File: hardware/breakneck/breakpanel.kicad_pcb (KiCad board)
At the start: 2 copper layers, 145 x 165 mm, 690 parts, among them J1 CONN_WEST, J10 GS2, J12 CONN_JTAG_6P, J15 GS2, J16 CONN_JST, J2 CONN_DEDI, J3 CONN_OLED, J4 USB_C_Receptacle, J5 CONN_SOUTH, J6 CONN_EAST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

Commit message: Flushed current changes to accommodate results of recent assembly tests; Introduced plastics engineering resources, made fiducial marks SMT for placing, merged SMT attribute to panel design accordingly, removed incomplete test point symbol, and sanitised private file path.
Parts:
- FID2 (x6), FID4 (x6), FID6 (x5): footprint Monero_Local:Fiducial_1mm_Dia_2.54mm_Outer_CopperBottom -> Monero_Local:Fiducial_1mm_Dia_2.54mm_Outer_CopperTop; moved to B.Cu
- turned FID2 to 270 degrees (x6)
- turned FID4 to 270 degrees (x6)
- turned FID6 to 270 degrees (x3)
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
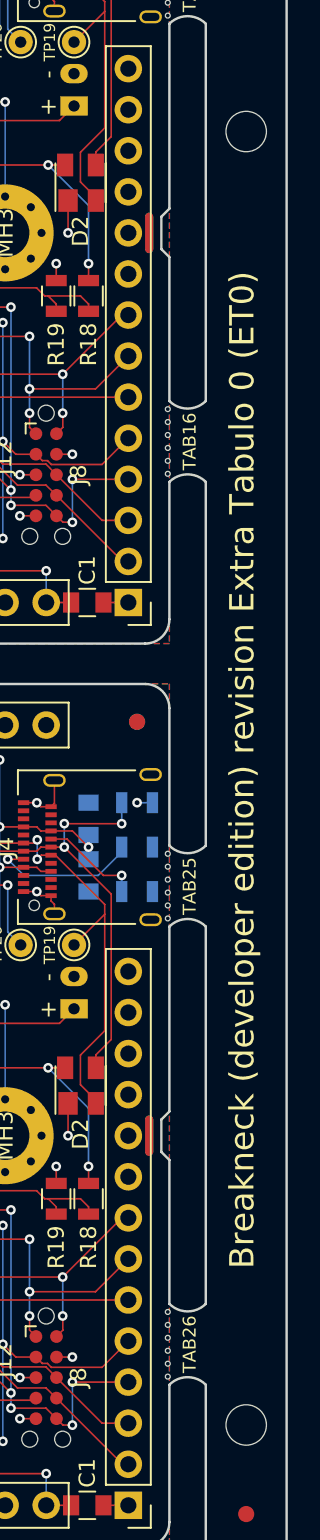
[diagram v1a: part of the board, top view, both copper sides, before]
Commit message: Completed USBC debugging structures, including removal of unused contacts, symbol adaptation, introduction of solderbridges, test point connections, and complete segregation of inner row USBC connector pads.
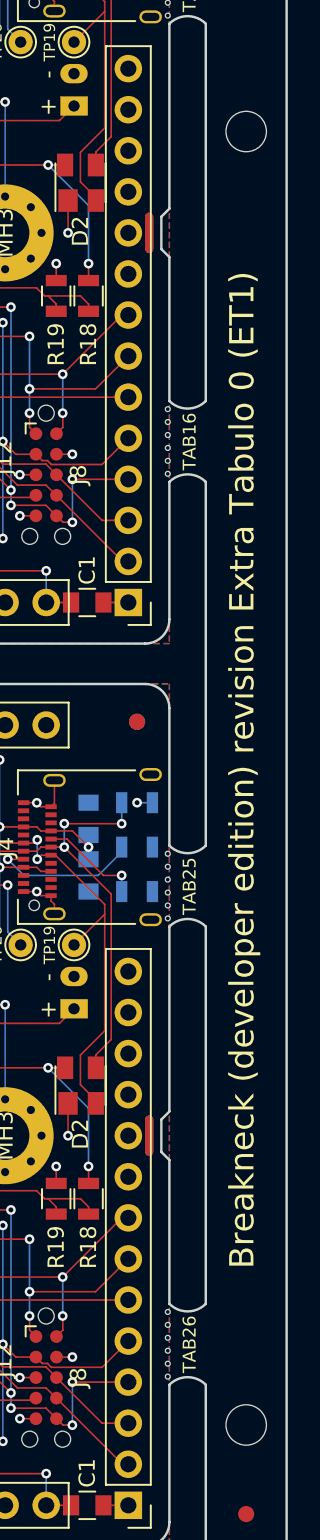
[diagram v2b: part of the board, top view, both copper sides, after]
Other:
- board text added: "Breakneck (developer edition) revision Extra Tabulo 0 (ET1)"
- board text added: "Fifth generation prototype RFC-HWALLET-1 ET1 Extra Tabulo, by the Monero Hardware Team CERN OSH License, © 2018 The Monero Project"
- board text removed: "Breakneck (developer edition) revision Extra Tabulo 0 (ET0)"
- board text removed: "Fifth generation prototype RFC-HWALLET-1 ET0 Extra Tabulo, by the Monero Hardware Team CERN OSH License, © 2018 The Monero Project"
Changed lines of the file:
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@@
     (title "Breakneck Hardware Wallet")
     (date 2018-01-10)
-    (rev 0.9.0)
+    (rev 0.9.1)
     (company "The Monero Project, Hardware Team")
     (comment 1 "Copyright © 2018, The Monero Project")
@@
     (effects (font (size 1.5 1.5) (thickness 0.3)))
   )
-  (gr_text "Breakneck (developer edition) revision Extra Tabulo 0 (ET0)" (at 165 137 90) (layer F.SilkS)
+  (gr_text "Breakneck (developer edition) revision Extra Tabulo 0 (ET1)" (at 165 137 90) (layer F.SilkS)
     (effects (font (size 1.5 1.5) (thickness 0.3)))
   )
@@
   (gr_line (start 36 132.68) (end 34 132.68) (angle 90) (layer Edge.Cuts) (width 0.15))
   (gr_line (start 34 132.68) (end 33 131.68) (angle 90) (layer Edge.Cuts) (width 0.15))
-  (gr_text "Fifth generation prototype RFC-HWALLET-1\nET0 Extra Tabulo, by the Monero Hardware Team\nCERN OSH License, © 2018 The Monero Project" (at 53 140.02 90) (layer B.SilkS)
+  (gr_text "Fifth generation prototype RFC-HWALLET-1\nET1 Extra Tabulo, by the Monero Hardware Team\nCERN OSH License, © 2018 The Monero Project" (at 53 140.02 90) (layer B.SilkS)
     (effects (font (size 1 1) (thickness 0.2)) (justify left mirror))
   )
@@
   (gr_line (start 102.5 132.68) (end 100.5 132.68) (angle 90) (layer Edge.Cuts) (width 0.15))
   (gr_line (start 100.5 132.68) (end 99.5 131.68) (angle 90) (layer Edge.Cuts) (width 0.15))
-  (gr_text "Fifth generation prototype RFC-HWALLET-1\nET0 Extra Tabulo, by the Monero Hardware Team\nCERN OSH License, © 2018 The Monero Project" (at 119.5 140.02 90) (layer B.SilkS)
+  (gr_text "Fifth generation prototype RFC-HWALLET-1\nET1 Extra Tabulo, by the Monero Hardware Team\nCERN OSH License, © 2018 The Monero Project" (at 119.5 140.02 90) (layer B.SilkS)
     (effects (font (size 1 1) (thickness 0.2)) (justify left mirror))
   )
@@
   (gr_line (start 102.5 76.84) (end 100.5 76.84) (angle 90) (layer Edge.Cuts) (width 0.15))
   (gr_line (start 100.5 76.84) (end 99.5 75.84) (angle 90) (layer Edge.Cuts) (width 0.15))
-  (gr_text "Fifth generation prototype RFC-HWALLET-1\nET0 Extra Tabulo, by the Monero Hardware Team\nCERN OSH License, © 2018 The Monero Project" (at 119.5 84.18 90) (layer B.SilkS)
+  (gr_text "Fifth generation prototype RFC-HWALLET-1\nET1 Extra Tabulo, by the Monero Hardware Team\nCERN OSH License, © 2018 The Monero Project" (at 119.5 84.18 90) (layer B.SilkS)
     (effects (font (size 1 1) (thickness 0.2)) (justify left mirror))
   )
@@
   (gr_line (start 160 48.94) (end 160 46.94) (angle 90) (layer Edge.Cuts) (width 0.15))
   (gr_line (start 160 46.94) (end 160.5 46.44) (angle 90) (layer Edge.Cuts) (width 0.15))
-  (gr_text "Fifth generation prototype RFC-HWALLET-1\nET0 Extra Tabulo, by the Monero Hardware Team\nCERN OSH License, © 2018 The Monero Project" (at 119.5 28.34 90) (layer B.SilkS)
+  (gr_text "Fifth generation prototype RFC-HWALLET-1\nET1 Extra Tabulo, by the Monero Hardware Team\nCERN OSH License, © 2018 The Monero Project" (at 119.5 28.34 90) (layer B.SilkS)
     (effects (font (size 1 1) (thickness 0.2)) (justify left mirror))
   )
@@
   (gr_line (start 36 21) (end 34 21) (angle 90) (layer Edge.Cuts) (width 0.15))
   (gr_line (start 34 21) (end 33 20) (angle 90) (layer Edge.Cuts) (width 0.15))
-  (gr_text "Fifth generation prototype RFC-HWALLET-1\nET0 Extra Tabulo, by the Monero Hardware Team\nCERN OSH License, © 2018 The Monero Project" (at 53 28.34 90) (layer B.SilkS)
+  (gr_text "Fifth generation prototype RFC-HWALLET-1\nET1 Extra Tabulo, by the Monero Hardware Team\nCERN OSH License, © 2018 The Monero Project" (at 53 28.34 90) (layer B.SilkS)
     (effects (font (size 1 1) (thickness 0.2)) (justify left mirror))
   )
@@
     (effects (font (size 1 1) (thickness 0.15)))
   )
-  (gr_text "Fifth generation prototype RFC-HWALLET-1\nET0 Extra Tabulo, by the Monero Hardware Team\nCERN OSH License, © 2018 The Monero Project" (at 53 84.18 90) (layer B.SilkS)
+  (gr_text "Fifth generation prototype RFC-HWALLET-1\nET1 Extra Tabulo, by the Monero Hardware Team\nCERN OSH License, © 2018 The Monero Project" (at 53 84.18 90) (layer B.SilkS)
     (effects (font (size 1 1) (thickness 0.2)) (justify left mirror))
   )

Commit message: Bumped revision identifiers and legal text pending new year of the pig.
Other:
- board text added: "Panelised by the Monero Hardware team, January 2019"
- board text added: "Seventh generation prototype RFC-HWALLET-1 ET1 Extra Tabulo, by the Monero Hardware Team CERN OSH License, © 2019 The Monero Project"
- board text removed: "Fifth generation prototype RFC-HWALLET-1 ET1 Extra Tabulo, by the Monero Hardware Team CERN OSH License, © 2018 The Monero Project"
- board text removed: "Panelised by the Monero Hardware team, 6 December 2018"
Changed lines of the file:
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@@
     (title "Breakneck Hardware Wallet")
     (date 2018-01-10)
-    (rev 0.9.1)
+    (rev 0.9.2)
     (company "The Monero Project, Hardware Team")
-    (comment 1 "Copyright © 2018, The Monero Project")
+    (comment 1 "Copyright © 2019, The Monero Project")
     (comment 2 "Fulfilling the developer edition role")
     (comment 3 "Pending quality assurance testing")
@@
     (effects (font (size 1.5 1.5) (thickness 0.3)))
   )
-  (gr_text "Panelised by the Monero Hardware team, 6 December 2018" (at 25 138 90) (layer F.SilkS)
+  (gr_text "Panelised by the Monero Hardware team, January 2019" (at 25 138 90) (layer F.SilkS)
     (effects (font (size 1.5 1.5) (thickness 0.3)))
   )
@@
   (gr_line (start 36 132.68) (end 34 132.68) (angle 90) (layer Edge.Cuts) (width 0.15))
   (gr_line (start 34 132.68) (end 33 131.68) (angle 90) (layer Edge.Cuts) (width 0.15))
-  (gr_text "Fifth generation prototype RFC-HWALLET-1\nET1 Extra Tabulo, by the Monero Hardware Team\nCERN OSH License, © 2018 The Monero Project" (at 53 140.02 90) (layer B.SilkS)
+  (gr_text "Seventh generation prototype RFC-HWALLET-1\nET1 Extra Tabulo, by the Monero Hardware Team\nCERN OSH License, © 2019 The Monero Project" (at 53 140.02 90) (layer B.SilkS)
     (effects (font (size 1 1) (thickness 0.2)) (justify left mirror))
   )
@@
   (gr_line (start 102.5 132.68) (end 100.5 132.68) (angle 90) (layer Edge.Cuts) (width 0.15))
   (gr_line (start 100.5 132.68) (end 99.5 131.68) (angle 90) (layer Edge.Cuts) (width 0.15))
-  (gr_text "Fifth generation prototype RFC-HWALLET-1\nET1 Extra Tabulo, by the Monero Hardware Team\nCERN OSH License, © 2018 The Monero Project" (at 119.5 140.02 90) (layer B.SilkS)
+  (gr_text "Seventh generation prototype RFC-HWALLET-1\nET1 Extra Tabulo, by the Monero Hardware Team\nCERN OSH License, © 2019 The Monero Project" (at 119.5 140.02 90) (layer B.SilkS)
     (effects (font (size 1 1) (thickness 0.2)) (justify left mirror))
   )
@@
   (gr_line (start 102.5 76.84) (end 100.5 76.84) (angle 90) (layer Edge.Cuts) (width 0.15))
   (gr_line (start 100.5 76.84) (end 99.5 75.84) (angle 90) (layer Edge.Cuts) (width 0.15))
-  (gr_text "Fifth generation prototype RFC-HWALLET-1\nET1 Extra Tabulo, by the Monero Hardware Team\nCERN OSH License, © 2018 The Monero Project" (at 119.5 84.18 90) (layer B.SilkS)
+  (gr_text "Seventh generation prototype RFC-HWALLET-1\nET1 Extra Tabulo, by the Monero Hardware Team\nCERN OSH License, © 2019 The Monero Project" (at 119.5 84.18 90) (layer B.SilkS)
     (effects (font (size 1 1) (thickness 0.2)) (justify left mirror))
   )
@@
   (gr_line (start 160 48.94) (end 160 46.94) (angle 90) (layer Edge.Cuts) (width 0.15))
   (gr_line (start 160 46.94) (end 160.5 46.44) (angle 90) (layer Edge.Cuts) (width 0.15))
-  (gr_text "Fifth generation prototype RFC-HWALLET-1\nET1 Extra Tabulo, by the Monero Hardware Team\nCERN OSH License, © 2018 The Monero Project" (at 119.5 28.34 90) (layer B.SilkS)
+  (gr_text "Seventh generation prototype RFC-HWALLET-1\nET1 Extra Tabulo, by the Monero Hardware Team\nCERN OSH License, © 2019 The Monero Project" (at 119.5 28.34 90) (layer B.SilkS)
     (effects (font (size 1 1) (thickness 0.2)) (justify left mirror))
   )
@@
   (gr_line (start 36 21) (end 34 21) (angle 90) (layer Edge.Cuts) (width 0.15))
   (gr_line (start 34 21) (end 33 20) (angle 90) (layer Edge.Cuts) (width 0.15))
-  (gr_text "Fifth generation prototype RFC-HWALLET-1\nET1 Extra Tabulo, by the Monero Hardware Team\nCERN OSH License, © 2018 The Monero Project" (at 53 28.34 90) (layer B.SilkS)
+  (gr_text "Seventh generation prototype RFC-HWALLET-1\nET1 Extra Tabulo, by the Monero Hardware Team\nCERN OSH License, © 2019 The Monero Project" (at 53 28.34 90) (layer B.SilkS)
     (effects (font (size 1 1) (thickness 0.2)) (justify left mirror))
   )
@@
     (effects (font (size 1 1) (thickness 0.15)))
   )
-  (gr_text "Fifth generation prototype RFC-HWALLET-1\nET1 Extra Tabulo, by the Monero Hardware Team\nCERN OSH License, © 2018 The Monero Project" (at 53 84.18 90) (layer B.SilkS)
+  (gr_text "Seventh generation prototype RFC-HWALLET-1\nET1 Extra Tabulo, by the Monero Hardware Team\nCERN OSH License, © 2019 The Monero Project" (at 53 84.18 90) (layer B.SilkS)
     (effects (font (size 1 1) (thickness 0.2)) (justify left mirror))
   )

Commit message: Corrected fiducial placement on wrong side of board panel.
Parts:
- FID6: footprint Monero_Local:Fiducial_1mm_Dia_2.54mm_Outer_CopperBottom -> Monero_Local:Fiducial_1mm_Dia_2.54mm_Outer_CopperTop; moved to B.Cu
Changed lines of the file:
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@@
     )
   )
-  (module Monero_Local:Fiducial_1mm_Dia_2.54mm_Outer_CopperBottom (layer F.Cu)
+  (module Monero_Local:Fiducial_1mm_Dia_2.54mm_Outer_CopperTop (layer B.Cu)
     (at 92 22.34 90)
     (descr "Circular Fiducial, 1mm bare copper bottom; 2.54mm keepout")
